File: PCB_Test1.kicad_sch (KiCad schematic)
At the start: 8 parts, among them IC101 L70REL-M37-EIT, Q101 DTC143Z

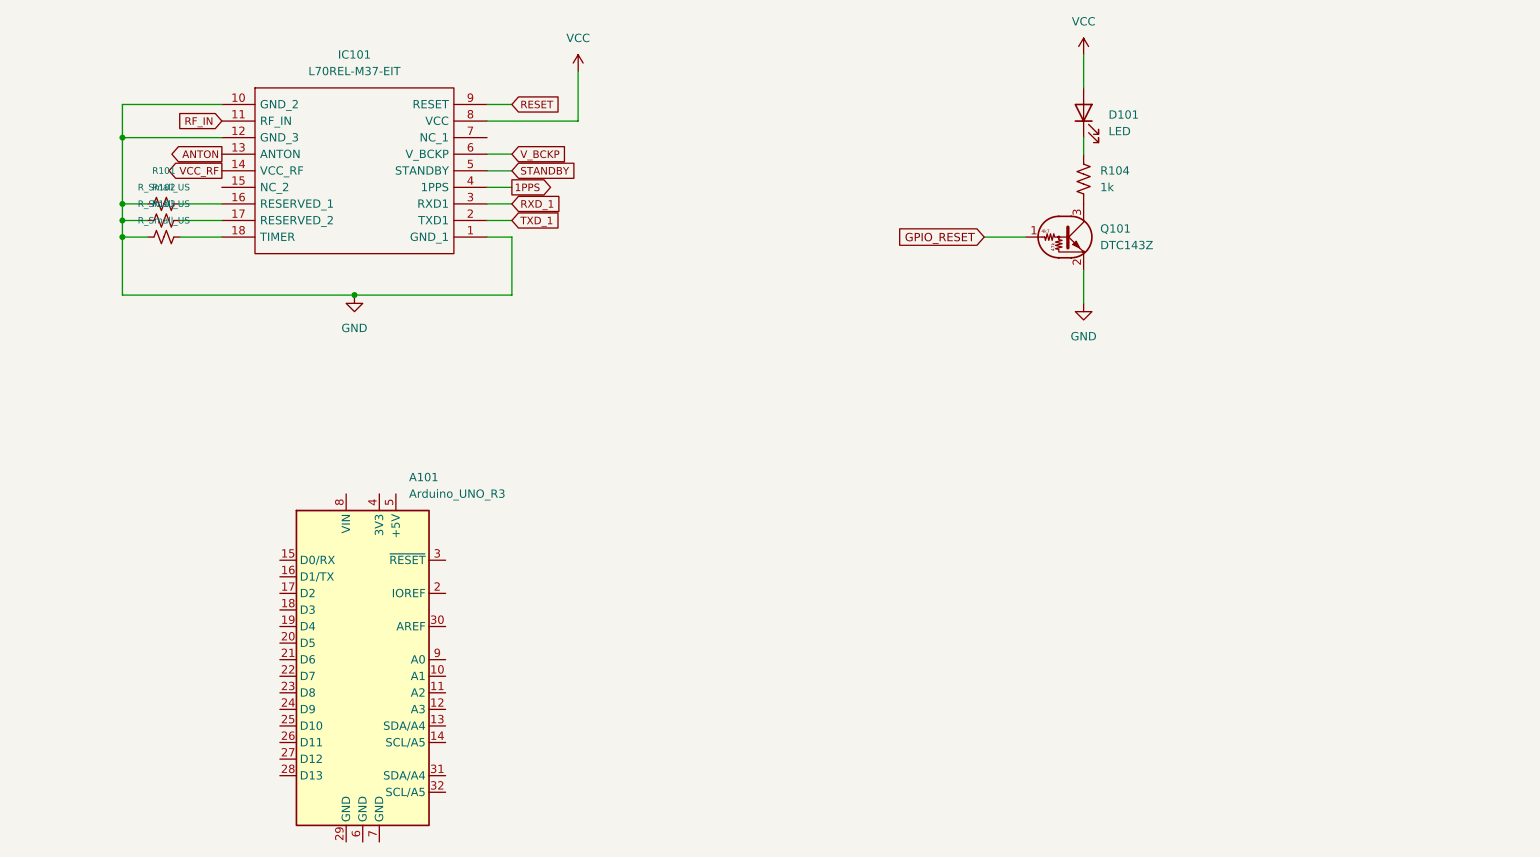
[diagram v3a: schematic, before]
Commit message: Added male headers for arduino uno r3
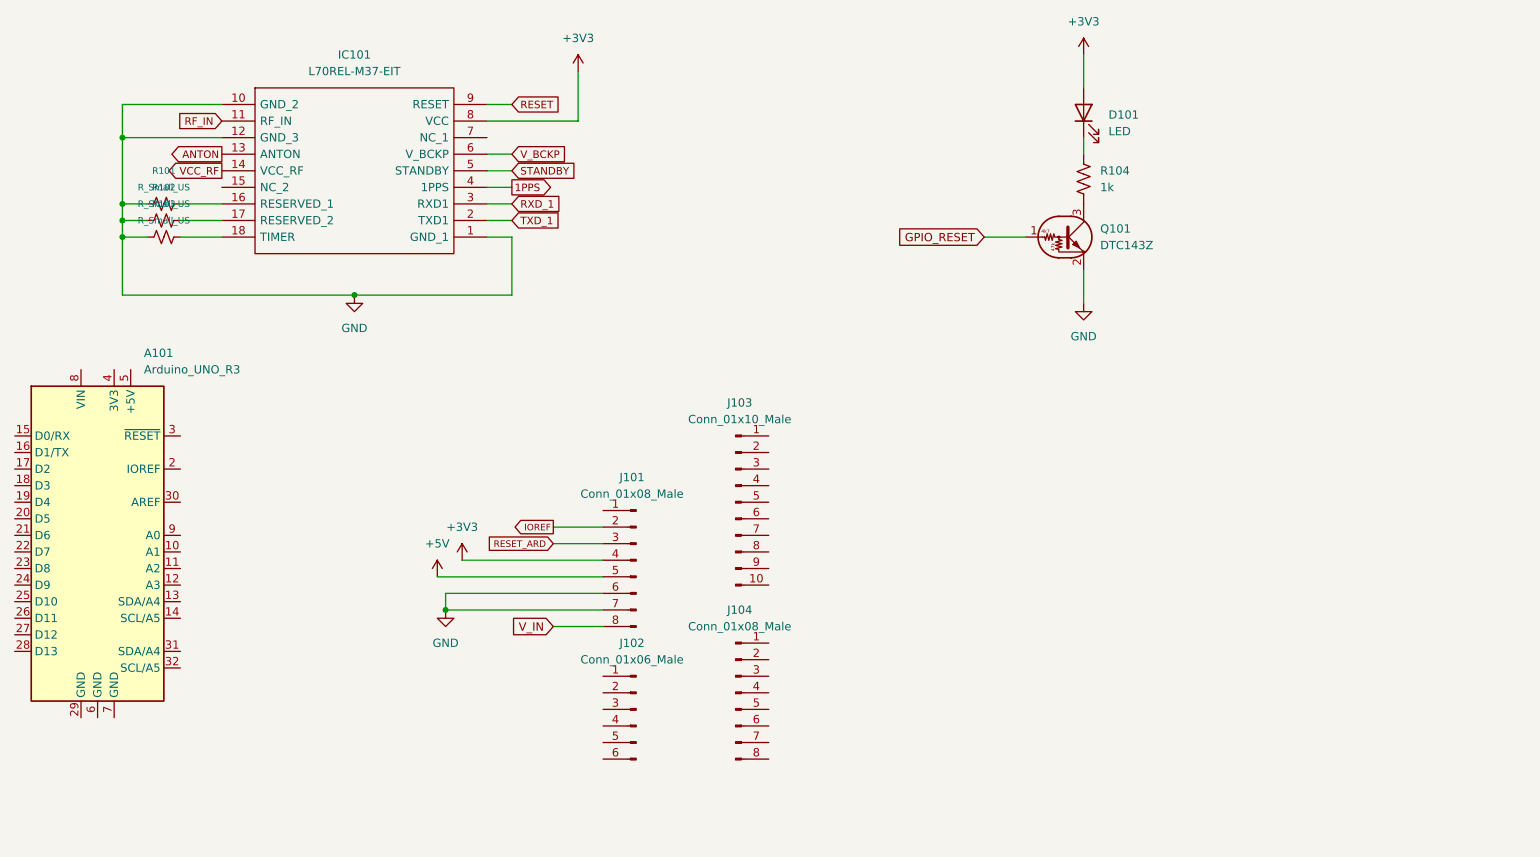
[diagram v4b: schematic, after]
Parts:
- added J101, J104: Conn_01x08_Male, Connector_PinHeader_2.54mm:PinHeader_1x08_P2.54mm_Vertical, symbol Connector:Conn_01x08_Male
- added J102: Conn_01x06_Male, Connector_PinHeader_2.54mm:PinHeader_1x06_P2.54mm_Vertical, symbol Connector:Conn_01x06_Male
- added J103: Conn_01x10_Male, Connector_PinHeader_2.54mm:PinHeader_1x10_P2.54mm_Vertical, symbol Connector:Conn_01x10_Male
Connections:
- net GND: now also J101.6 (Pin_6), J101.7 (Pin_7)
- net VCC renamed +3V3
- net +3V3: now also J101.4 (Pin_4)
- new net +5V: J101.5 (Pin_5)
- new net IOREF: J101.2 (Pin_2)
- new net RESET_ARD: J101.3 (Pin_3)
- new net V_IN: J101.8 (Pin_8)
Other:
- moved on the sheet: A101

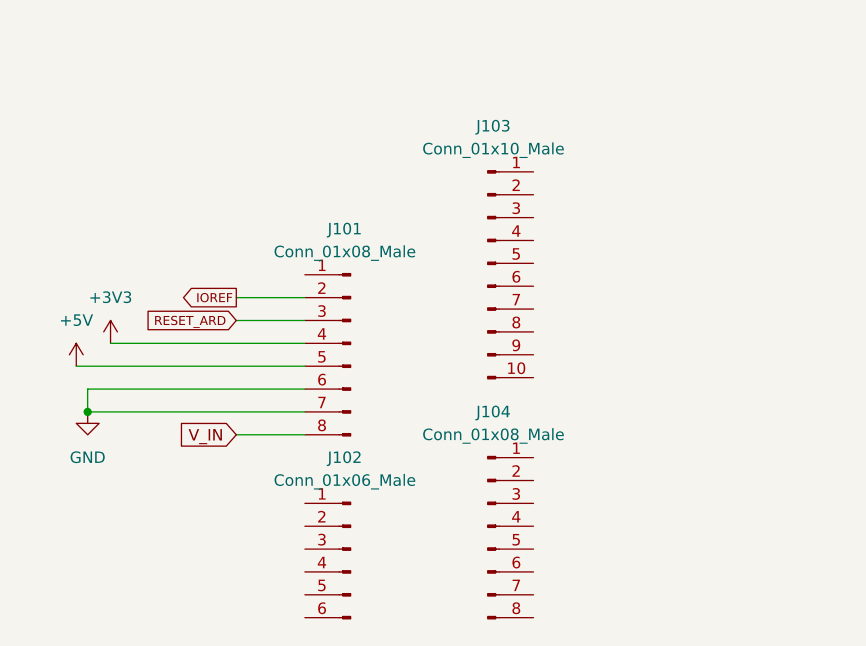
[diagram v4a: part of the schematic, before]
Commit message: Add nets to all header pins
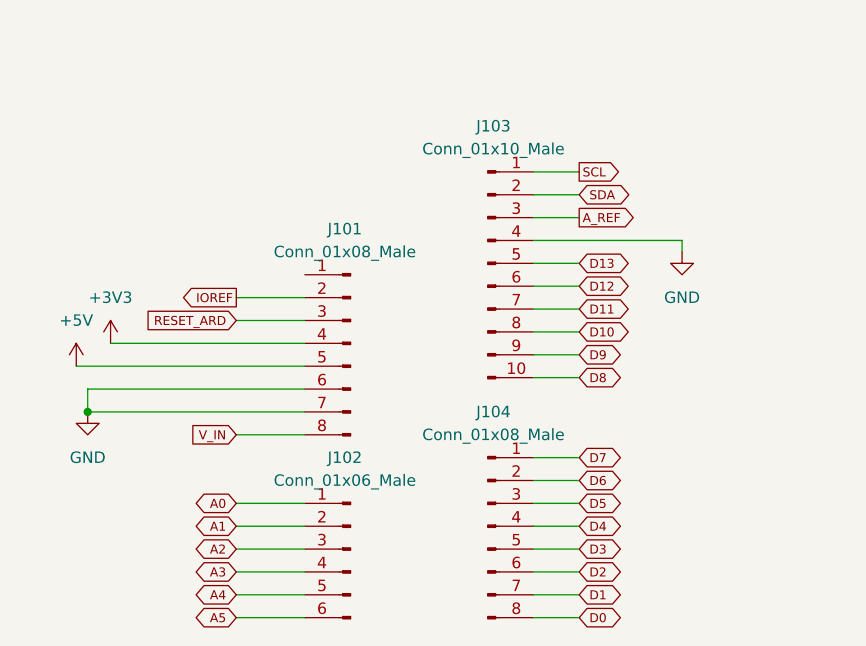
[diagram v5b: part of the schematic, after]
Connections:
- net GND: now also J103.4 (Pin_4)
- net A0: now reaches J102.1 (Pin_1)
- net A1: now reaches J102.2 (Pin_2)
- net A2: now reaches J102.3 (Pin_3)
- net A3: now reaches J102.4 (Pin_4)
- net A4: now reaches J102.5 (Pin_5)
- net A5: now reaches J102.6 (Pin_6)
- net SCL: now reaches J103.1 (Pin_1)
- net D8: now reaches J103.10 (Pin_10)
- net SDA: now reaches J103.2 (Pin_2)
- net A_REF: now reaches J103.3 (Pin_3)
- net D13: now reaches J103.5 (Pin_5)
- net D12: now reaches J103.6 (Pin_6)
- net D11: now reaches J103.7 (Pin_7)
- net D10: now reaches J103.8 (Pin_8)
- net D9: now reaches J103.9 (Pin_9)
- net D7: now reaches J104.1 (Pin_1)
- net D6: now reaches J104.2 (Pin_2)
- net D5: now reaches J104.3 (Pin_3)
- net D4: now reaches J104.4 (Pin_4)
- net D3: now reaches J104.5 (Pin_5)
- net D2: now reaches J104.6 (Pin_6)
- net D1: now reaches J104.7 (Pin_7)
- net D0: now reaches J104.8 (Pin_8)

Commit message: minor changes
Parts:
- added Q?: DTC143Z, Package_TO_SOT_SMD:SOT-416, symbol Transistor_BJT:DTC143Z
- IC101: value L70REL-M37-EIT -> L70REL-M37
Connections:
- net D2 is gone; now on net GPIO_RESET: J104.6 (Pin_6)
- net 1PPS: now also Q101.1 (B)
- net GND: now also Q?.2 (E)
- net GPIO_RESET: now also Q?.1 (B); no longer Q101.1 (B)
- net RESET: now also Q?.3 (C)
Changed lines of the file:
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@@
+    (stroke (width 0) (type default) (color 0 0 0 0))
+  )
+  (wire (pts (xy 238.76 55.88) (xy 238.76 63.5))
     (stroke (width 0) (type default) (color 0 0 0 0))
   )
@@
     (stroke (width 0) (type default) (color 0 0 0 0))
   )
+  (wire (pts (xy 223.52 68.58) (xy 229.87 68.58))
+    (stroke (width 0) (type default) (color 0 0 0 0))
+  )
   (wire (pts (xy 139.7 115.57) (xy 134.62 115.57))
     (stroke (width 0) (type default) (color 0 0 0 0))
@@
     (stroke (width 0) (type default) (color 0 0 0 0))
   )
-  (wire (pts (xy 182.88 39.37) (xy 182.88 44.45))
+  (wire (pts (xy 182.88 41.91) (xy 182.88 44.45))
     (stroke (width 0) (type default) (color 0 0 0 0))
   )
@@
   )
   (wire (pts (xy 95.25 54.61) (xy 91.44 54.61))
+    (stroke (width 0) (type default) (color 0 0 0 0))
+  )
+  (wire (pts (xy 238.76 73.66) (xy 238.76 78.74))
     (stroke (width 0) (type default) (color 0 0 0 0))
   )
@@
     )
   )
+  (global_label "GPIO_RESET" (shape input) (at 223.52 68.58 180) (fields_autoplaced)
+    (effects (font (size 1.27 1.27)) (justify right))
+    (property "Intersheet References" "${INTERSHEET_REFS}" (id 0) (at 209.9188 68.5006 0)
+      (effects (font (size 1.27 1.27)) (justify right) hide)
+    )
+  )
   (global_label "ANTON" (shape output) (at 50.8 54.61 180) (fields_autoplaced)
     (effects (font (size 1.15 1.15)) (justify right))
@@
     )
   )
+  (global_label "RESET" (shape output) (at 238.76 55.88 90) (fields_autoplaced)
+    (effects (font (size 1.15 1.15)) (justify left))
+    (property "Intersheet References" "${INTERSHEET_REFS}" (id 0) (at 238.6881 48.4925 90)
+      (effects (font (size 1.15 1.15)) (justify left) hide)
+    )
+  )
   (global_label "A3" (shape bidirectional) (at 101.6 142.24 180) (fields_autoplaced)
     (effects (font (size 1 1)) (justify right))
@@
     )
   )
-  (global_label "GPIO_RESET" (shape input) (at 167.64 67.31 180) (fields_autoplaced)
+  (global_label "1PPS" (shape input) (at 167.64 67.31 180) (fields_autoplaced)
     (effects (font (size 1.27 1.27)) (justify right))
-    (property "Intersheet References" "${INTERSHEET_REFS}" (id 0) (at 154.0388 67.2306 0)
+    (property "Intersheet References" "${INTERSHEET_REFS}" (id 0) (at 160.2679 67.2306 0)
       (effects (font (size 1.27 1.27)) (justify right) hide)
     )
@@
     )
   )
-  (global_label "D2" (shape bidirectional) (at 139.7 142.24 0) (fields_autoplaced)
-    (effects (font (size 1 1)) (justify left))
-    (property "Intersheet References" "${INTERSHEET_REFS}" (id 0) (at 143.5524 142.1775 0)
+  (global_label "GPIO_RESET" (shape output) (at 139.7 142.24 0) (fields_autoplaced)
+    (effects (font (size 1 1)) (justify left))
+    (property "Intersheet References" "${INTERSHEET_REFS}" (id 0) (at 150.4095 142.1775 0)
       (effects (font (size 1 1)) (justify left) hide)
     )
@@
       (effects (font (size 1 1)) (justify left) hide)
     )
+  )
+  (symbol (lib_id "Transistor_BJT:DTC143Z") (at 236.22 68.58 0) (unit 1)
+    (in_bom yes) (on_board yes) (fields_autoplaced)
+    (property "Reference" "Q?" (id 0) (at 241.3 67.3099 0)
+      (effects (font (size 1.27 1.27)) (justify left))
+    )
+    (property "Value" "DTC143Z" (id 1) (at 241.3 69.8499 0)
+      (effects (font (size 1.27 1.27)) (justify left))
+    )
+    (property "Footprint" "Package_TO_SOT_SMD:SOT-416" (id 2) (at 236.22 68.58 0)
+      (effects (font (size 1.27 1.27)) (justify left) hide)
+    )
+    (property "Datasheet" "" (id 3) (at 236.22 68.58 0)
+      (effects (font (size 1.27 1.27)) (justify left) hide)
+    )
+    (pin "1")
+    (pin "2")
+    (pin "3")
   )
   (symbol (lib_id "power:GND") (at 71.12 76.2 0) (unit 1)
@@
     (pin "1")
   )
+  (symbol (lib_id "power:GND") (at 238.76 78.74 0) (unit 1)
+    (in_bom yes) (on_board yes) (fields_autoplaced)
+    (property "Reference" "#PWR?" (id 0) (at 238.76 85.09 0)
+      (effects (font (size 1.27 1.27)) hide)
+    )
+    (property "Value" "GND" (id 1) (at 238.76 83.82 0))
+    (property "Footprint" "" (id 2) (at 238.76 78.74 0)
+      (effects (font (size 1.27 1.27)) hide)
+    )
+    (property "Datasheet" "" (id 3) (at 238.76 78.74 0)
+      (effects (font (size 1.27 1.27)) hide)
+    )
+    (pin "1")
+  )
   (symbol (lib_id "Device:R_Small_US") (at 41.91 67.31 90) (unit 1)
     (in_bom yes) (on_board yes)
@@
     (in_bom yes) (on_board yes) (fields_autoplaced)
     (property "Reference" "IC101" (id 0) (at 71.12 39.37 0))
-    (property "Value" "L70REL-M37-EIT" (id 1) (at 71.12 41.91 0))
+    (property "Value" "L70REL-M37" (id 1) (at 71.12 41.91 0))
     (property "Footprint" "L70REL-M37-EIT:L70RELM37EIT" (id 2) (at 87.63 44.45 0)
       (effects (font (size 1.27 1.27)) (justify left) hide)
@@
     (pin "1")
   )
-  (symbol (lib_id "power:+3V3") (at 182.88 39.37 0) (unit 1)
-    (in_bom yes) (on_board yes) (fields_autoplaced)
-    (property "Reference" "#PWR0107" (id 0) (at 182.88 43.18 0)
-      (effects (font (size 1.27 1.27)) hide)
-    )
-    (property "Value" "+3V3" (id 1) (at 182.88 34.29 0))
-    (property "Footprint" "" (id 2) (at 182.88 39.37 0)
-      (effects (font (size 1.27 1.27)) hide)
-    )
-    (property "Datasheet" "" (id 3) (at 182.88 39.37 0)
+  (symbol (lib_id "power:+3V3") (at 182.88 41.91 0) (unit 1)
+    (in_bom yes) (on_board yes) (fields_autoplaced)
+    (property "Reference" "#PWR0107" (id 0) (at 182.88 45.72 0)
+      (effects (font (size 1.27 1.27)) hide)
+    )
+    (property "Value" "+3V3" (id 1) (at 182.88 36.83 0))
+    (property "Footprint" "" (id 2) (at 182.88 41.91 0)
+      (effects (font (size 1.27 1.27)) hide)
+    )
+    (property "Datasheet" "" (id 3) (at 182.88 41.91 0)
       (effects (font (size 1.27 1.27)) hide)
     )
@@
       (reference "#PWR?") (unit 1) (value "GND") (footprint "")
     )
+    (path "/80afbcad-9187-4125-9e57-0c454bf2f130"
+      (reference "#PWR?") (unit 1) (value "GND") (footprint "")
+    )
     (path "/577d95df-df73-428a-8f02-e461f346fc7b"
       (reference "A101") (unit 1) (value "Arduino_UNO_R3") (footprint "Module:Arduino_UNO_R3")
@@
     )
     (path "/cf0bbd0d-22ee-4ea7-9877-80945221f044"
-      (reference "IC101") (unit 1) (value "L70REL-M37-EIT") (footprint "L70REL-M37-EIT:L70RELM37EIT")
+      (reference "IC101") (unit 1) (value "L70REL-M37") (footprint "L70REL-M37-EIT:L70RELM37EIT")
     )
     (path "/1f4c0749-3f34-407d-8579-75b20d59efc9"
@@
       (reference "Q101") (unit 1) (value "DTC143Z") (footprint "Package_TO_SOT_SMD:SOT-416")
     )
+    (path "/04a3d8b3-7f59-4804-a113-c442c2257647"
+      (reference "Q?") (unit 1) (value "DTC143Z") (footprint "Package_TO_SOT_SMD:SOT-416")
+    )
     (path "/4dc54989-4adb-4c88-ac5e-0741877f7a3c"
